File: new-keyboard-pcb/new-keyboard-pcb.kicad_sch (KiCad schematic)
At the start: 29 parts, among them J1 Conn_ARM_JTAG_SWD_10, J2 Conn_01x04_Socket, J3 Conn_01x04_Pin, J4 Conn_01x03_Socket, J5 Conn_01x03_Pin, J6 Conn_01x03_Socket, J7 Conn_01x03_Pin, SW100 SW_Push_Dual, U1 PRTR5V0U2X, U2 STM32F072CBTx, U3 AP2112K-3.3, Y1 8MHz

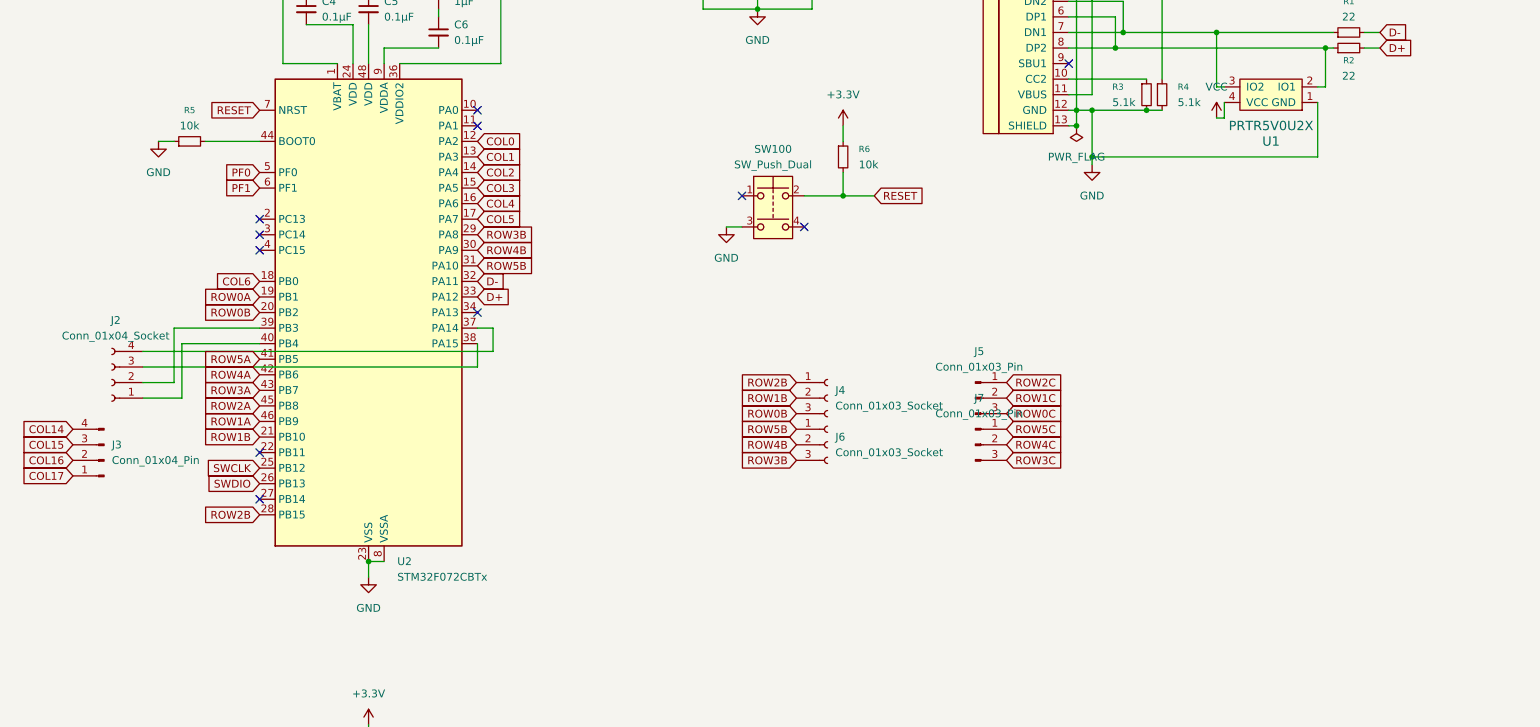
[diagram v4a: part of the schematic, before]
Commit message: new connectors placed
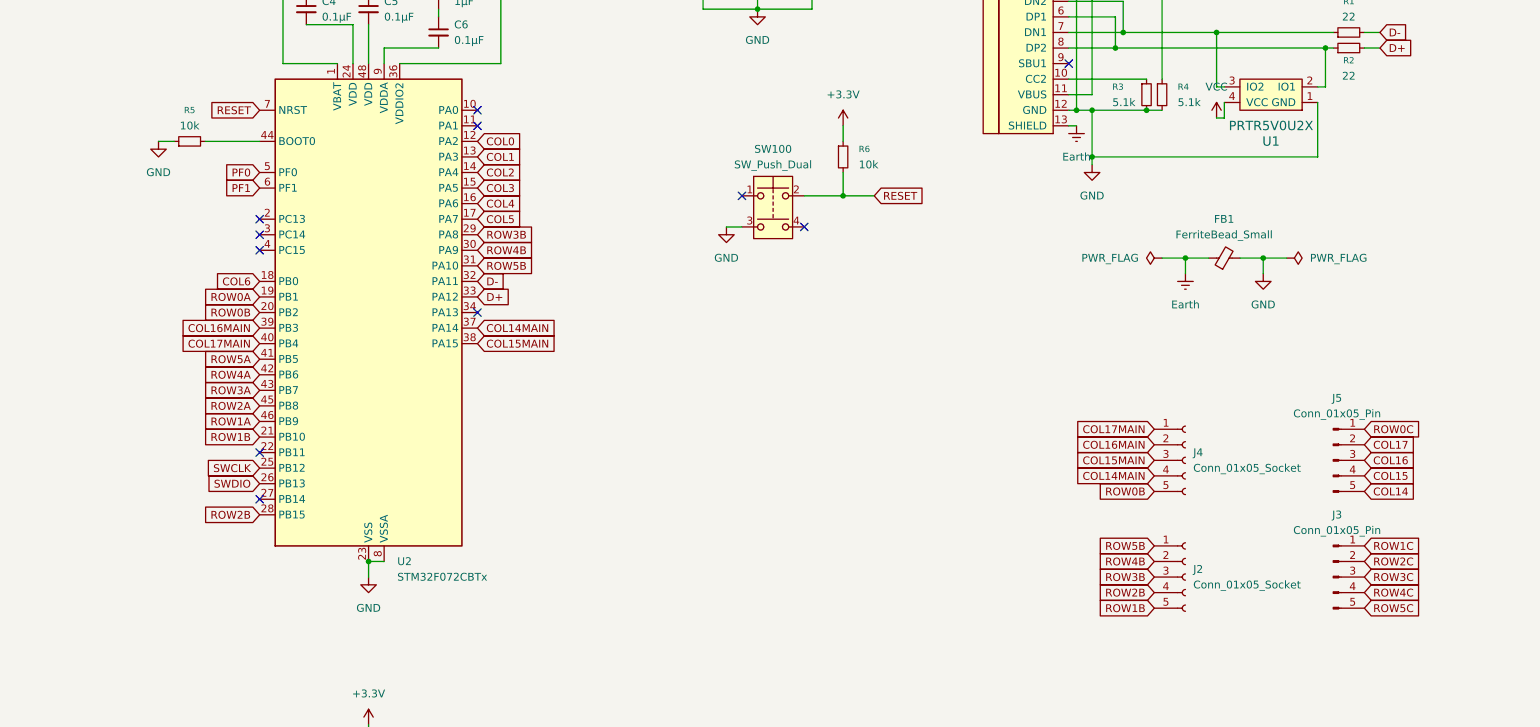
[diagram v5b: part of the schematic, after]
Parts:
- removed J2: Conn_01x04_Socket, pogo_conn_4_pins:686L0421350120E, symbol Connector:Conn_01x04_Socket
- removed J3: Conn_01x04_Pin, pogo_conn_4_pins:685L0421250110E, symbol Connector:Conn_01x04_Pin
- removed J4, J6: Conn_01x03_Socket, pogo_conn_3_pins:685F0321351124E, symbol Connector:Conn_01x03_Socket
- removed J5, J7: Conn_01x03_Pin, pogo_conn_3_pins:685F0321350124E, symbol Connector:Conn_01x03_Pin
- added FB1: FerriteBead_Small, Inductor_SMD:L_0805_2012Metric_Pad1.05x1.20mm_HandSolder, symbol Device:FerriteBead_Small
- added J2, J4: Conn_01x05_Socket, pogo_connector_5_pins:female, symbol Connector:Conn_01x05_Socket
- added J3, J5: Conn_01x05_Pin, pogo_connector_5_pins:male, symbol Connector:Conn_01x05_Pin
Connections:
- net COL14: now also J5.5 (Pin_5)
- net COL15: now also J5.4 (Pin_4)
- net COL16: now also J5.3 (Pin_3)
- net COL17: now also J5.2 (Pin_2)
- net GND: now also FB1.2; no longer USB1.13 (SHIELD)
- net ROW0B: now also J4.5 (Pin_5)
- net ROW0C: now also J5.1 (Pin_1)
- net ROW1B: now also J2.5 (Pin_5)
- net ROW1C: now also J3.1 (Pin_1)
- net ROW2B: now also J2.4 (Pin_4)
- net ROW2C: now also J3.2 (Pin_2)
- net ROW3B: now also J2.3 (Pin_3)
- net ROW3C: now also J3.3 (Pin_3)
- net ROW4B: now also J2.2 (Pin_2)
- net ROW4C: now also J3.4 (Pin_4)
- net ROW5B: now also J2.1 (Pin_1)
- net ROW5C: now also J3.5 (Pin_5)
- net COL14MAIN: now reaches U2.37 (PA14)
- net COL14MAIN: now also J4.4 (Pin_4)
- net COL15MAIN: now reaches U2.38 (PA15)
- net COL15MAIN: now also J4.3 (Pin_3)
- net COL16MAIN: now reaches U2.39 (PB3)
- net COL16MAIN: now also J4.2 (Pin_2)
- net COL17MAIN: now reaches U2.40 (PB4)
- net COL17MAIN: now also J4.1 (Pin_1)
- new net Earth: FB1.1, USB1.13 (SHIELD)

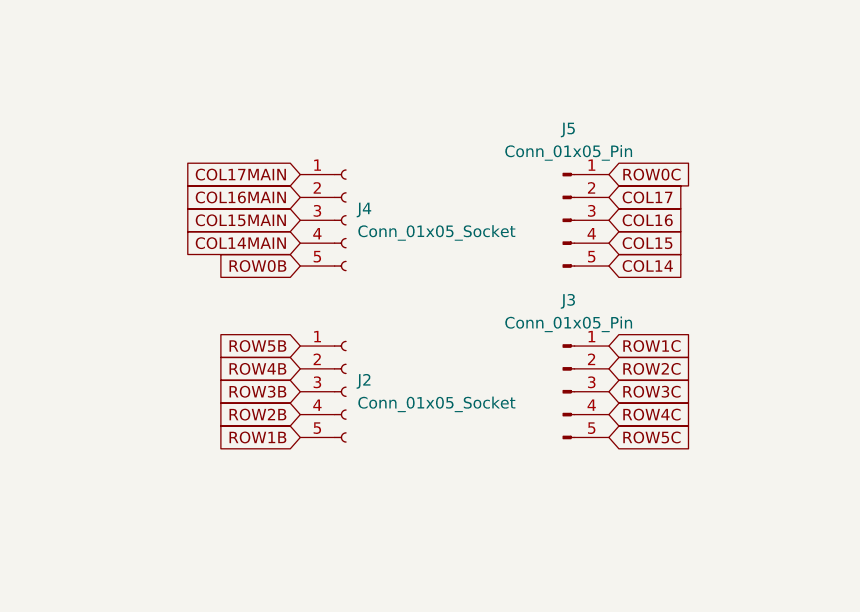
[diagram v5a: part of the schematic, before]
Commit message: Correcting pogo connector connexions
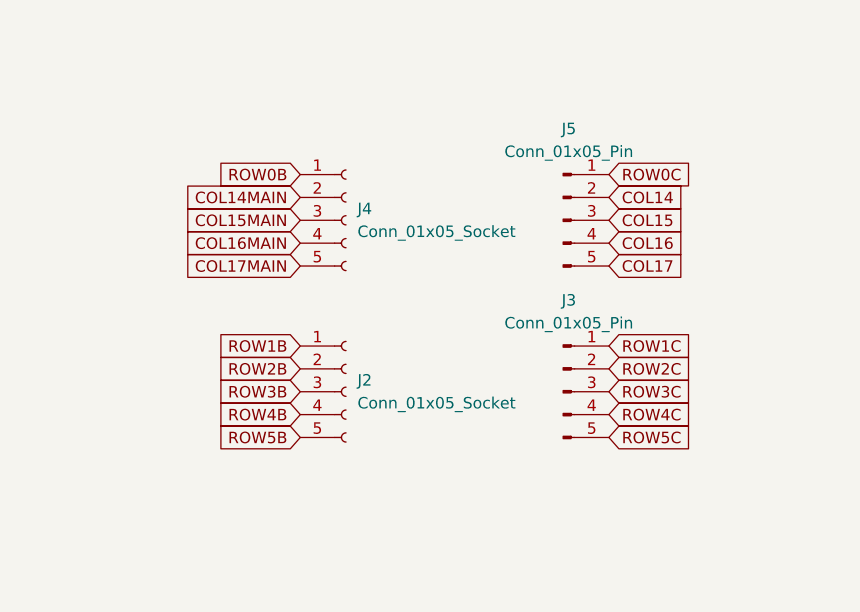
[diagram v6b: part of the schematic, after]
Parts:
- J2, J4: footprint pogo_connector_5_pins:female -> pogo_connector_5_pins:connector
- J3, J5: footprint pogo_connector_5_pins:male -> pogo_connector_5_pins:connector
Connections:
- net COL14: now also J5.2 (Pin_2); no longer J5.5 (Pin_5)
- net COL14MAIN: now also J4.2 (Pin_2); no longer J4.4 (Pin_4)
- net COL15: now also J5.3 (Pin_3); no longer J5.4 (Pin_4)
- net COL16: now also J5.4 (Pin_4); no longer J5.3 (Pin_3)
- net COL16MAIN: now also J4.4 (Pin_4); no longer J4.2 (Pin_2)
- net COL17: now also J5.5 (Pin_5); no longer J5.2 (Pin_2)
- net COL17MAIN: now also J4.5 (Pin_5); no longer J4.1 (Pin_1)
- net ROW0B: now also J4.1 (Pin_1); no longer J4.5 (Pin_5)
- net ROW1B: now also J2.1 (Pin_1); no longer J2.5 (Pin_5)
- net ROW2B: now also J2.2 (Pin_2); no longer J2.4 (Pin_4)
- net ROW4B: now also J2.4 (Pin_4); no longer J2.2 (Pin_2)
- net ROW5B: now also J2.5 (Pin_5); no longer J2.1 (Pin_1)
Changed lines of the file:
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@@
 	(global_label "COL16MAIN"
 		(shape input)
-		(at 198.12 109.22 180)
+		(at 198.12 114.3 180)
 		(fields_autoplaced yes)
 		(effects
@@
 		)
 		(property "Intersheetrefs" "${INTERSHEET_REFS}"
-			(at 184.6119 109.22 0)
+			(at 184.6119 114.3 0)
 			(effects
 				(font
@@
 	(global_label "COL17MAIN"
 		(shape input)
-		(at 198.12 106.68 180)
+		(at 198.12 116.84 180)
 		(fields_autoplaced yes)
 		(effects
@@
 		)
 		(property "Intersheetrefs" "${INTERSHEET_REFS}"
-			(at 184.6119 106.68 0)
+			(at 184.6119 116.84 0)
 			(effects
 				(font
@@
 	(global_label "COL16"
 		(shape input)
-		(at 232.41 111.76 0)
+		(at 232.41 114.3 0)
 		(fields_autoplaced yes)
 		(effects
@@
 		)
 		(property "Intersheetrefs" "${INTERSHEET_REFS}"
-			(at 241.4428 111.76 0)
+			(at 241.4428 114.3 0)
 			(effects
 				(font
@@
 	(global_label "COL17"
 		(shape input)
-		(at 232.41 109.22 0)
+		(at 232.41 116.84 0)
 		(fields_autoplaced yes)
 		(effects
@@
 		)
 		(property "Intersheetrefs" "${INTERSHEET_REFS}"
-			(at 241.4428 109.22 0)
+			(at 241.4428 116.84 0)
 			(effects
 				(font
@@
 	(global_label "ROW0B"
 		(shape input)
-		(at 198.12 116.84 180)
+		(at 198.12 106.68 180)
 		(fields_autoplaced yes)
 		(effects
@@
 		)
 		(property "Intersheetrefs" "${INTERSHEET_REFS}"
-			(at 188.6034 116.84 0)
+			(at 188.6034 106.68 0)
 			(effects
 				(font
@@
 	(global_label "ROW5B"
 		(shape input)
-		(at 198.12 125.73 180)
+		(at 198.12 135.89 180)
 		(fields_autoplaced yes)
 		(effects
@@
 		)
 		(property "Intersheetrefs" "${INTERSHEET_REFS}"
-			(at 188.6034 125.73 0)
+			(at 188.6034 135.89 0)
 			(effects
 				(font
@@
 	(global_label "COL14"
 		(shape input)
-		(at 232.41 116.84 0)
+		(at 232.41 109.22 0)
 		(fields_autoplaced yes)
 		(effects
@@
 		)
 		(property "Intersheetrefs" "${INTERSHEET_REFS}"
-			(at 241.4428 116.84 0)
+			(at 241.4428 109.22 0)
 			(effects
 				(font
@@
 	(global_label "ROW4B"
 		(shape input)
-		(at 198.12 128.27 180)
+		(at 198.12 133.35 180)
 		(fields_autoplaced yes)
 		(effects
@@
 		)
 		(property "Intersheetrefs" "${INTERSHEET_REFS}"
-			(at 188.6034 128.27 0)
+			(at 188.6034 133.35 0)
 			(effects
 				(font
@@
 	(global_label "ROW2B"
 		(shape input)
-		(at 198.12 133.35 180)
+		(at 198.12 128.27 180)
 		(fields_autoplaced yes)
 		(effects
@@
 		)
 		(property "Intersheetrefs" "${INTERSHEET_REFS}"
-			(at 188.6034 133.35 0)
+			(at 188.6034 128.27 0)
 			(effects
 				(font
@@
 	(global_label "ROW1B"
 		(shape input)
-		(at 198.12 135.89 180)
+		(at 198.12 125.73 180)
 		(fields_autoplaced yes)
 		(effects
@@
 		)
 		(property "Intersheetrefs" "${INTERSHEET_REFS}"
-			(at 188.6034 135.89 0)
+			(at 188.6034 125.73 0)
 			(effects
 				(font
@@
 	(global_label "COL15"
 		(shape input)
-		(at 232.41 114.3 0)
+		(at 232.41 111.76 0)
 		(fields_autoplaced yes)
 		(effects
@@
 		)
 		(property "Intersheetrefs" "${INTERSHEET_REFS}"
-			(at 241.4428 114.3 0)
+			(at 241.4428 111.76 0)
 			(effects
 				(font
@@
 	(global_label "COL14MAIN"
 		(shape input)
-		(at 198.12 114.3 180)
+		(at 198.12 109.22 180)
 		(fields_autoplaced yes)
 		(effects
@@
 		)
 		(property "Intersheetrefs" "${INTERSHEET_REFS}"
-			(at 184.6119 114.3 0)
+			(at 184.6119 109.22 0)
 			(effects
 				(font
@@
 			)
 		)
-		(property "Footprint" "pogo_connector_5_pins:male"
+		(property "Footprint" "pogo_connector_5_pins:connector"
 			(at 227.33 130.81 0)
 			(effects
@@
 			)
 		)
-		(property "Footprint" "pogo_connector_5_pins:female"
+		(property "Footprint" "pogo_connector_5_pins:connector"
 			(at 203.2 111.76 0)
 			(effects
@@
 			)
 		)
-		(property "Footprint" "pogo_connector_5_pins:male"
+		(property "Footprint" "pogo_connector_5_pins:connector"
 			(at 227.33 111.76 0)
 			(effects
@@
 			)
 		)
-		(property "Footprint" "pogo_connector_5_pins:female"
+		(property "Footprint" "pogo_connector_5_pins:connector"
 			(at 203.2 130.81 0)
 			(effects
